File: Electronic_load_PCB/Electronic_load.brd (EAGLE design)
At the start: 121.9 x 100 mm, 70 parts, among them IC2 7805TV, J1 XT60-M, Q1 IRFP250, Q2 IRFP250, Q3 IRFP250, Q4 IRFP250, U1 ANALOG_DEVICES_AD8630ARZ-REEL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, U2 MCP4725A0T-E/CH, U3 ADS1115, U4 ATMEGA328P-AU, U5 OPA277-SOIC08, U6 MCP79410-I/SN, U7 ICL7660CPAZ

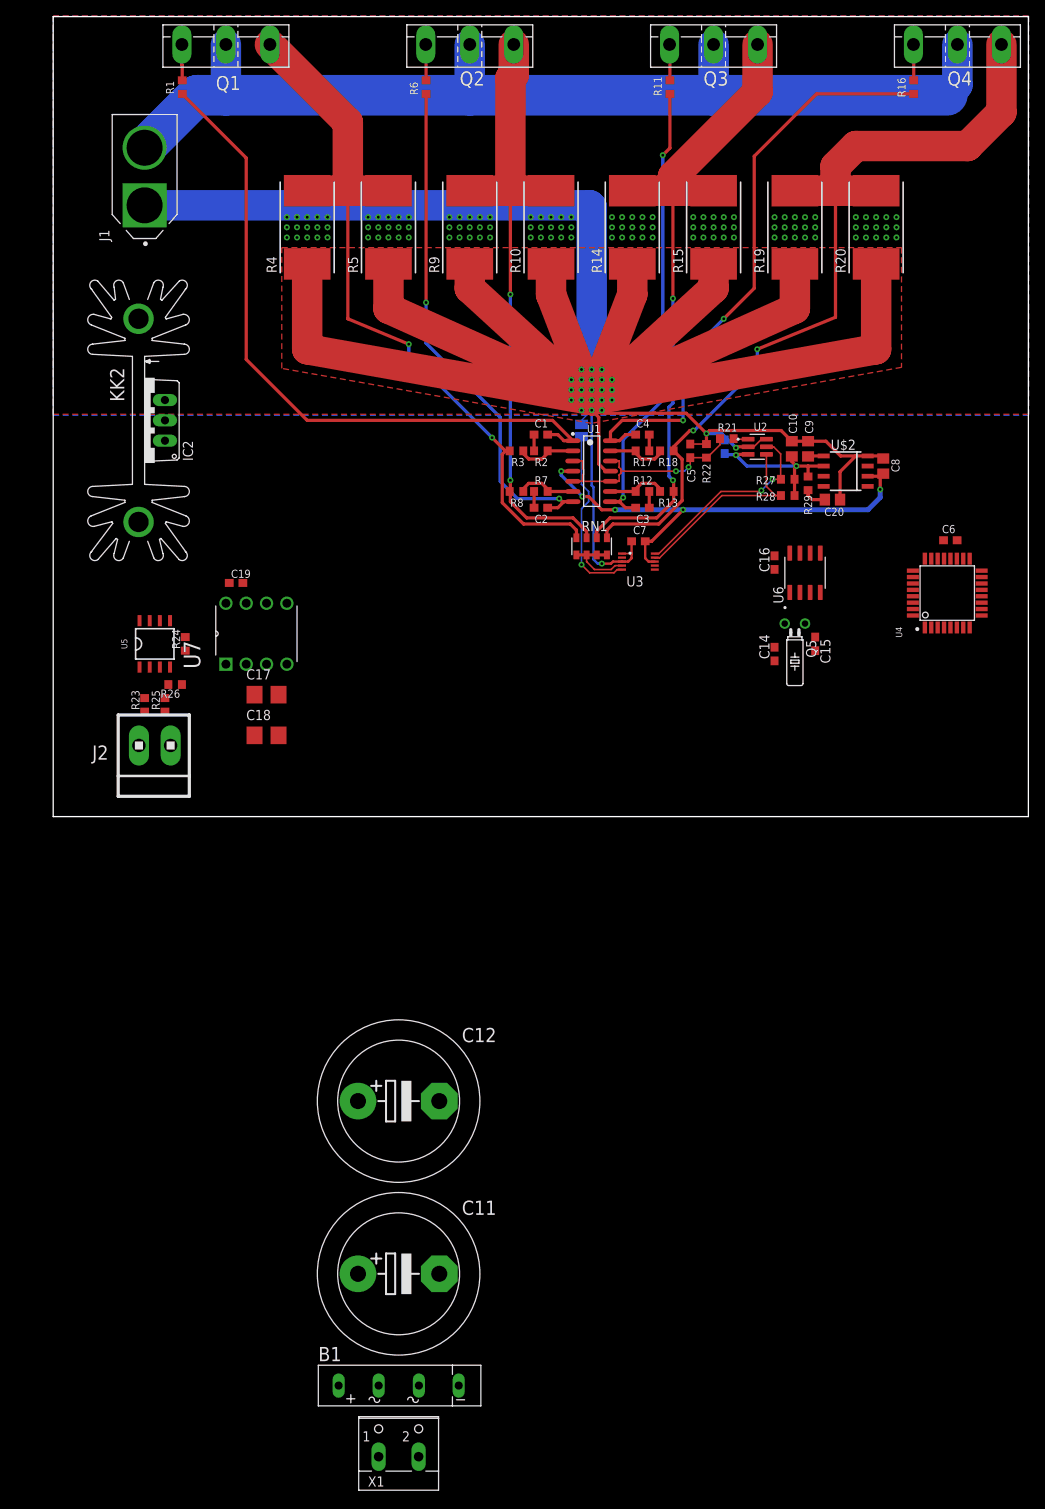
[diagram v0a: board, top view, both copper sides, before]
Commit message: Power supply schematic done
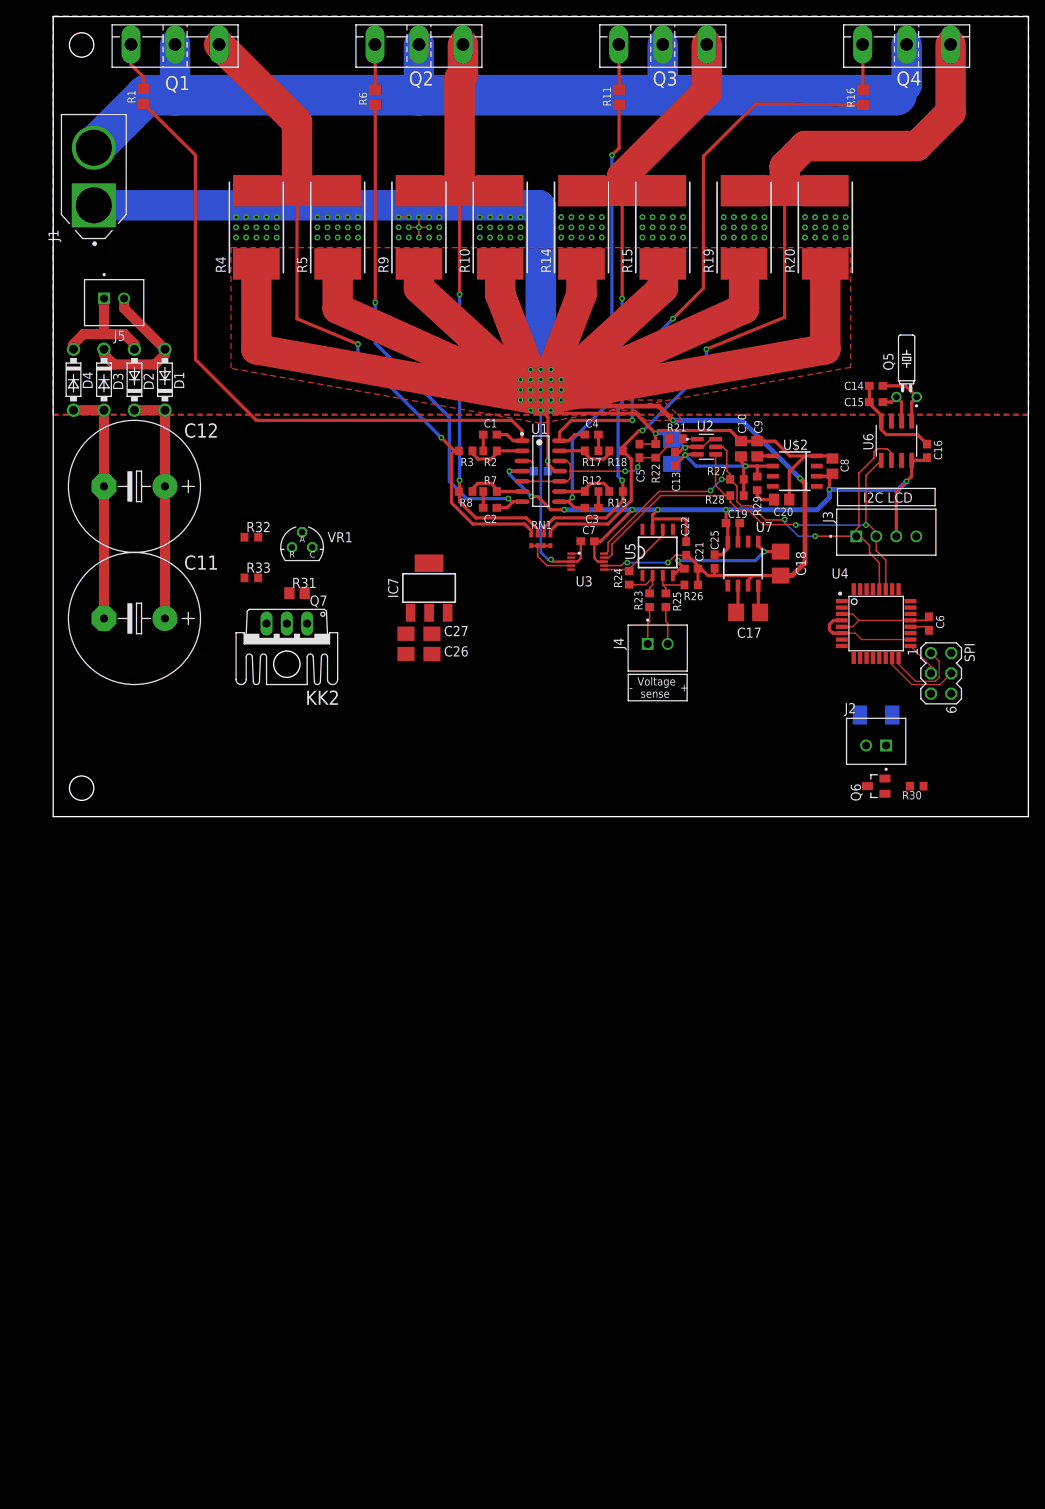
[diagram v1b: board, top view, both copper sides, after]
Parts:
- removed B1: (no value), rectifier:FB15
- removed IC2: 7805TV, linear:TO220V
- removed SJ1: (no value), jumper:SJ
- removed X1: (no value), con-wago-500:W237-102
- added C21, C22: 100n, rcl:C0603
- added C23: 100n, rcl:C0603K
- added C24: 10u, rcl:CT3528
- added C25: 1u, rcl:C0603
- added C26, C27: 10u, rcl:B/3528-21W
- added D1, D2, D3, D4: 1N5819-B, diode:DO41-7.6
- added IC7: LM1117IMPX-5.0, lm1117:SOT223
- added J3: B4B-XH-A(LF)(SN), B4B-XH-A_LF__SN_:JST_B4B-XH-A(LF)(SN)
- added J4, J5: B2B-XH-A(LF)(SN), JST_B2B-XH-A_LF__SN_:JST_B2B-XH-A(LF)(SN)
- added Q6: IRLML6244, IRLML6244:SOT23
- added Q7: BD911, BD911:TO220V
- added R30: (no value), rcl:R0603
- added R31: 1R, rcl:R0805
- added R32, R33: 1R, rcl:R0603
- added SPI: (no value), con-lstb:MA03-2
- added U$3: BYG22B, BYG22B:DO-214AC
- added VR1: (no value), tl431:TO92-CLP
- C11, C12: value (none) -> 4700u; device rcl:EB20D -> rcl:E7,5-16
- C14, C15: value (none) -> 6-9p
- C17, C18: value 10u -> 100u
- J2: value (none) -> B2B-XH-A(LF)(SN); device con-amp:1X2MTA -> JST_B2B-XH-A_LF__SN_:JST_B2B-XH-A(LF)(SN)
- KK2: value SK104-PAD -> SK95-2M3; device heatsink:SK104-PAD -> heatsink:SK95-2M3
- R1, R11, R16, R6: value 100 -> 1k; device rcl:R0603 -> rcl:R0805
- R10, R14, R15, R19, R20, R4, R5, R9: value (none) -> 0R2
- R23, R25: value (none) -> 1M
- R24, R26: value (none) -> 10k
- RN1: value (none) -> 1k; device resistor-dil:EXBS8V -> resistor-dil:CAT16
- U7: value ICL7660CPAZ -> ICL7660CPAZSOIC; device ICL7660CPAZ:DIP254P762X533-8 -> ICL7660CPAZ:SOIC8
- moved J2 90.2 mm to (102.9, 8.89), turned to 0 degrees
- moved C11 88.3 mm to (10.2, 24.8), turned to 180 degrees
- moved C12 83.6 mm to (10.2, 41.3), turned to 180 degrees
- moved C18 67.8 mm to (90.9, 31.6), turned to 90 degrees
- moved R26 65.7 mm to (79.8, 29.0)
- moved R23 64.5 mm to (74.5, 27.1)
- moved R25 64.0 mm to (76.6, 27.1)
- moved U5 63.9 mm to (75.6, 33.0)
- moved C19 62.6 mm to (85.0, 36.7)
- moved C17 61.1 mm to (86.9, 25.5)
- moved U7 57.2 mm to (86.2, 31.6), turned to 0 degrees
- moved R24 56.1 mm to (72.0, 29.8)
- moved C14 35.9 mm to (102.9, 53.8), turned to 180 degrees
- moved KK2 33.1 mm to (29.2, 21.6), turned to 180 degrees
- moved Q5 31.6 mm to (106.7, 52.5), turned to 0 degrees
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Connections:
- net N$1 renamed DAC_OUT
- net N$7 renamed AREF
- removed net N$12: SJ1.1, U3.5
- removed net N$29: B1.+, C11.+, C12.+
- removed net VOLTAGE-: U3.7
- new net +5V: SPI.2
- new net FAN: R30.1
- new net MISO: SPI.1, U4.16
- new net MOSI: SPI.4, U4.15
- new net N$1: Q7.1, R31.2, VR1.C
- new net N$30: Q6.1, R30.2
- new net N$38: R32.2, R33.1, VR1.R
- new net N$7: C11.+, C12.+, D1.C, D2.C, Q7.2, R31.1
- new net RST: SPI.5, U4.29
- new net SCK: SPI.3, U4.17
- net -5V: now also C21.1
- net 12V: now also C26.+, IC7.3, J2.1, Q7.3, R32.1, U$3.C; no longer IC2.1
- net 4,5V: now also C24.+
- net 5V: now also C22.2, C23.1, C25.1, C27.+, IC7.2, IC7.TAB, J3.3; no longer IC2.3
- net CURRENT: now also RN1.5, RN1.6, RN1.7, RN1.8; no longer RN1.1, RN1.2, RN1.3, RN1.4
- net CURRENT1: now also RN1.4; no longer RN1.8
- net CURRENT2: now also RN1.3; no longer RN1.7
- net CURRENT3: now also RN1.2; no longer RN1.6
- net CURRENT4: now also RN1.1; no longer RN1.5
- net GND: now also C21.2, C22.1, C23.2, C24.-, C25.2, C26.-, C27.-, D3.A, D4.A, IC7.1, J3.4, Q6.2, R33.2, SPI.6, U3.7, VR1.A; no longer B1.-, IC2.2, SJ1.2
- net N$24: now also J2.2, Q6.3, U$3.A; no longer R24.2, U5.6
- net N$25: now also J4.2; no longer J2.2
- net N$26: now also J4.1; no longer J2.1
- net N$27: now also D1.A, D3.C, J5.2; no longer B1.AC1, X1.1
- net N$28: now also D2.A, D4.C, J5.1; no longer B1.AC2, X1.2
- net SCL: now also J3.1
- net SDA: now also J3.2
- net VOLTAGE+: now also R24.2, U5.6
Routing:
- net GND: track 434.2 -> 575.3 mm, vias 144 -> 149
- net 5V: track 59.4 -> 114.7 mm, vias 5 -> 8
- net SCL: track 25.0 -> 68.8 mm, vias 2 -> 4
- net SDA: track 24.6 -> 62.5 mm, vias 0 -> 2
- net N$7: track 0.00 -> 29.8 mm
- net N$12: track 22.4 -> 0.00 mm, vias 1 -> 0
- net N$27: track 0.00 -> 18.4 mm
- net -5V: track 0.00 -> 18.0 mm, vias 0 -> 2
- net N$28: track 0.00 -> 14.4 mm
- net MISO: track 0.00 -> 10.4 mm
- net VOLTAGE+: track 0.00 -> 10.1 mm
- net MOSI: track 0.00 -> 9.86 mm
- net N$33: track 0.00 -> 8.08 mm
- net N$14: track 0.00 -> 5.65 mm
- net N$34: track 0.00 -> 5.22 mm
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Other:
- outline, holes or cut-outs redrawn
- board text added: "+"
- board text added: "-"
- board text added: "I2C LCD"
- board text added: "Voltage sense"

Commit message: finished power supply, added keypad, programming connector, transient trigger and more
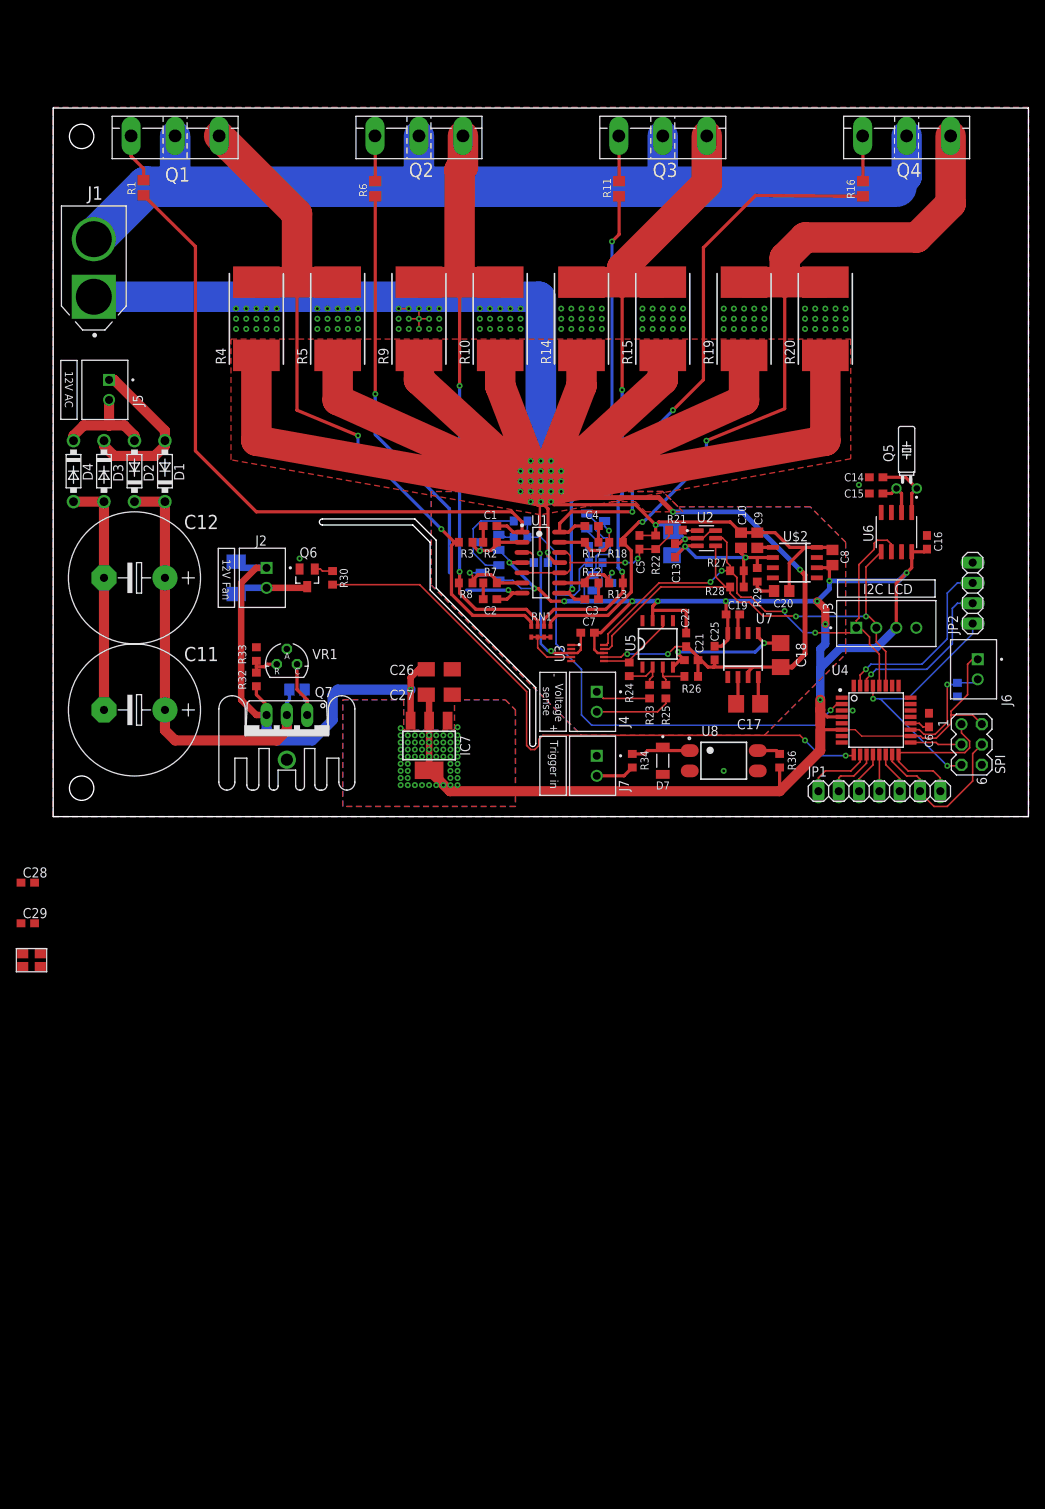
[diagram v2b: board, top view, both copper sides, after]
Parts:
- removed KK2: SK95-2M3, heatsink:SK95-2M3
- removed U$3: BYG22B, BYG22B:DO-214AC
- added C28, C29: 22p, rcl:C0603
- added D5: BYG22B, BYG22B:DO-214AC
- added D7: LL4148, diode:DIOMELF3515N
- added J6, J7: B2B-XH-A(LF)(SN), JST_B2B-XH-A_LF__SN_:JST_B2B-XH-A(LF)(SN)
- added JP1: (no value), pinhead:1X07
- added JP2: (no value), pinhead:1X04
- added Q10, Q11, Q8, Q9: MMBTA56-SOT23, transistor-pnp:SOT23
- added Q12: CRYSTAL_3,4X2,7, CRYSTAL_SMD_3,4x2.7mm:CRYSTAL_3,4X2,7
- added R34, R35, R36: 10k, rcl:R0603
- added R37, R38, R39, R40: 1k, rcl:R0603
- added U$1: TO220_HEATSINK, custom_heatsink:TO220_HEATSINK
- added U8: PC817X2NIP0F, PC817X2NIP0F:SOT254P975X400-4N
- R31: value 1R -> 100R
- R32, R33: value 1R -> 1k
- moved J2 79.0 mm to (26.7, 29.8), turned to 90 degrees
- moved R30 77.5 mm to (34.9, 29.8), turned to 90 degrees
- moved Q6 75.7 mm to (31.8, 29.8), turned to 180 degrees
- moved IC7 19.7 mm to (47.0, 8.89), turned to 180 degrees
- moved R32 17.8 mm to (25.4, 17.1), turned to 90 degrees
- moved VR1 14.7 mm to (29.2, 19.1)
- moved R31 12.1 mm to (30.5, 15.9), flipped to the bottom, turned to 180 degrees
- moved C6 12.1 mm to (109.5, 12.1)
- moved U4 12.1 mm to (102.9, 12.1)
- moved J5 11.4 mm to (6.99, 53.3), turned to 90 degrees
- moved C24 11.4 mm to (77.3, 34.2)
- moved J1 11.4 mm to (5.08, 68.6)
- moved Q1 11.4 mm to (15.2, 87.6)
- moved Q2 11.4 mm to (45.7, 87.6)
- moved Q3 11.4 mm to (76.2, 87.6)
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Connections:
- net N$1 renamed BASE
- net N$7 renamed 16V
- removed net +5V: SPI.2
- removed net MISO: SPI.1, U4.16
- removed net MOSI: SPI.4, U4.15
- new net KP1: JP1.1, U4.10
- new net KP2: JP1.2, U4.11
- new net KP3: JP1.3, U4.12
- new net KP4: JP1.4, U4.13
- new net KP5: JP1.5, U4.14
- new net KP6/MOSI: JP1.6, SPI.4, U4.15
- new net KP7/MISO: JP1.7, SPI.1, U4.16
- new net N$1: D7.C, R34.1, U8.1
- new net N$12: Q8.1, R37.2
- new net N$29: C28.1, Q12.CRST1
- new net N$37: Q9.1, R38.2
- new net N$39: C29.1, Q12.CRST2
- new net N$40: Q10.1, R39.2
- new net N$42: Q11.1, R40.2
- new net N$7: J7.2, R34.2
- new net OFF: R37.1, R38.1, R39.1, R40.1, U4.2
- new net RX: JP2.2, U4.30
- new net TEMP: J6.2, R35.2, U4.19
- new net TRIGG: R36.1, U8.4
- new net TX: JP2.3, U4.31
- new net XTL1: U4.7
- new net XTL2: U4.8
- net 12V: now also D5.C; no longer U$3.C
- net 5V: now also J6.1, Q10.2, Q11.2, Q8.2, Q9.2, R36.2, SPI.2
- net FAN: now also U4.9
- net GND: now also C28.2, C29.2, D7.A, J7.1, JP2.4, Q12.GND, Q12.GND2, R35.1, U8.2, U8.3
- net N$13: now also Q9.3
- net N$18: now also Q10.3
- net N$23: now also Q11.3
- net N$24: now also D5.A; no longer U$3.A
- net N$27: now also J5.1; no longer J5.2
- net N$28: now also J5.2; no longer J5.1
- net N$6: now also Q8.3
- net RST: now also JP2.1
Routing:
- net 5V: track 114.7 -> 256.9 mm, vias 8 -> 70
- net FAN: track 0.00 -> 79.9 mm, vias 0 -> 2
- net OFF: track 0.00 -> 71.6 mm, vias 0 -> 1
- net 12V: track 0.00 -> 63.5 mm, vias 0 -> 1
- net RST: track 0.00 -> 32.4 mm, vias 0 -> 2
- net 16V: track 29.8 -> 53.9 mm
- net TX: track 0.00 -> 23.5 mm, vias 0 -> 1
- net KP7/MISO: track 0.00 -> 21.2 mm
- net RX: track 0.00 -> 20.6 mm, vias 0 -> 1
- net KP6/MOSI: track 0.00 -> 20.6 mm
- net GND: track 575.3 -> 559.3 mm, vias 149 -> 154
- net TEMP: track 0.00 -> 14.2 mm, vias 0 -> 1
- net N$37: track 0.00 -> 12.3 mm
- net MISO: track 10.4 -> 0.00 mm
- net BASE: track 0.00 -> 10.2 mm
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- added copper zone on layer 1, net 5V
- added copper zone on layer 16, net 5V
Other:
- board size 121.9 x 100 mm -> 121.9 x 88.6 mm
- board text added: "12V AC"
- board text added: "12V Fan"
- board text added: "Trigger in"

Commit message: before voltage reference change
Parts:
- removed RN1: 1k, resistor-dil:CAT16
- added R41, R42, R43, R44: (no value), rcl:R0603
- Q10, Q11, Q8, Q9: value MMBTA56-SOT23 -> S9015; device transistor-pnp:SOT23 -> transistors:SOT23
- Q5: value (none) -> 32768Hz
- moved Q12 109.2 mm to (101.6, 11.4), flipped to the bottom, turned to 270 degrees
- moved C28 107.7 mm to (102.4, 13.5), flipped to the bottom
- moved C29 107.5 mm to (102.4, 7.24), flipped to the bottom, turned to 180 degrees
- moved C27 1.27 mm to (48.3, 16.5)
- moved C26 1.27 mm to (48.3, 19.7)
- moved IC7 1.27 mm to (47.0, 10.2)
- moved JP2 0.90 mm to (115.6, 28.6)
- moved SPI 0.68 mm to (114.2, 9.27)
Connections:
- removed net N$29: C28.1, Q12.CRST1
- removed net N$39: C29.1, Q12.CRST2
- new net T_GND: D7.A, J7.1, U8.2
- net CURRENT: now also R41.1, R42.1, R43.1, R44.1; no longer RN1.5, RN1.6, RN1.7, RN1.8
- net CURRENT1: now also R44.2; no longer RN1.4
- net CURRENT2: now also R43.2; no longer RN1.3
- net CURRENT3: now also R42.2; no longer RN1.2
- net CURRENT4: now also R41.2; no longer RN1.1
- net GND: no longer D7.A, J7.1, U8.2
- net XTL1: now also C28.1, Q12.CRST1
- net XTL2: now also C29.1, Q12.CRST2
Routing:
- net GND: track 559.3 -> 529.5 mm, vias 154 -> 155
- net XTL1: track 0.00 -> 10.6 mm, vias 0 -> 1
- net XTL2: track 0.00 -> 8.18 mm, vias 0 -> 1
- net CURRENT: track 8.41 -> 12.4 mm
- net T_GND: track 0.00 -> 3.55 mm, vias 0 -> 1
- net CURRENT1: track 94.7 -> 91.7 mm
- net N$10: track 60.3 -> 63.4 mm
- net CURRENT2: track 79.5 -> 77.7 mm
- net 12V: track 63.5 -> 64.7 mm
- net 5V: track 256.9 -> 258.2 mm
- net TX: track 23.5 -> 24.4 mm
- net RX: track 20.6 -> 21.5 mm
- net SCK: track 6.47 -> 5.74 mm
- net CURRENT3: track 84.2 -> 84.8 mm
- net CURRENT4: track 107.8 -> 107.3 mm
- added copper zone on layer 1, net T_GND
- added copper zone on layer 16, net T_GND
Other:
- outline, holes or cut-outs redrawn
- board text added: "DC Electronic Load V1.0 Dominik Workshop"

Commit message: new voltage reference
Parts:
- removed C10: 1u, rcl:C0805
- removed C20: 10u, rcl:C0805
- removed C24: 10u, rcl:CT3528
- removed R29: 1R, rcl:R0603
- removed U$2: REF5045IDSOIC, REF504x:SOIC8
- added U$3: LM4140, voltage_references:SOIC8
- C8: value 1u-10u -> 10u; device rcl:C0805 -> rcl:CT3528
- C9: device rcl:C0805 -> rcl:CT3216
- J2, J4, J5, J6, J7: value B2B-XH-A(LF)(SN) -> B2B-XH; device JST_B2B-XH-A_LF__SN_:JST_B2B-XH-A(LF)(SN) -> jst connectors:JST_B2B-XH-A(LF)(SN)
- J3: value B4B-XH-A(LF)(SN) -> B4B-XH; device B4B-XH-A_LF__SN_:JST_B4B-XH-A(LF)(SN) -> jst connectors:JST_B4B-XH-A(LF)(SN)
- moved C8 6.87 mm to (90.8, 34.3)
- moved C9 2.81 mm to (87.1, 37.2), turned to 270 degrees
- moved U6 1.42 mm to (106.7, 36.2)
- moved C14 1.42 mm to (104.1, 43.1)
- moved C15 1.42 mm to (104.1, 41.0)
- moved C16 1.42 mm to (110.5, 34.9)
- moved Q5 1.42 mm to (108.0, 41.7)
- moved R40 0.25 mm to (67.8, 34.0)
- moved Q10 0.25 mm to (68.6, 29.0)
- moved Q8 0.25 mm to (54.6, 34.5)
- moved R39 0.25 mm to (67.8, 32.0)
- moved Q11 0.13 mm to (67.8, 37.1)
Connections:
- removed net 4,5V: C10.1, C13.1, C24.+, R27.1, R28.1, R29.2, U$2.6, U2.3
- removed net N$19: C9.1, U$2.5
- removed net N$36: C20.1, R29.1
- new net 4,096V: C13.1, C9.+, R27.1, R28.1, U$3.6, U2.3
- net 5V: now also C8.+, U$3.2, U$3.3; no longer C8.1, U$2.2
- net GND: now also C8.-, C9.-, U$3.1, U$3.4, U$3.7, U$3.8; no longer C10.2, C20.2, C24.-, C8.2, C9.2, U$2.4
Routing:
- net 4,096V: track 0.00 -> 33.6 mm, vias 0 -> 2
- net GND: track 529.5 -> 497.9 mm, vias 155 -> 156
- net 4,5V: track 23.6 -> 0.00 mm, vias 2 -> 0
- net 5V: track 258.2 -> 278.0 mm
- net N$36: track 2.98 -> 0.00 mm
- net 12V: track 64.7 -> 61.9 mm
- net N$19: track 1.97 -> 0.00 mm
- net SCL: track 69.9 -> 71.5 mm
- net SDA: track 63.1 -> 64.3 mm
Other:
- outline, holes or cut-outs redrawn
